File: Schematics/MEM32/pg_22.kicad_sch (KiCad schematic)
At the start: 6 parts, among them U1806 XLRULOGIC, U1901 F244, U1903 TSXXPAL, U1907 F258, U1908 F258, U2908 F64

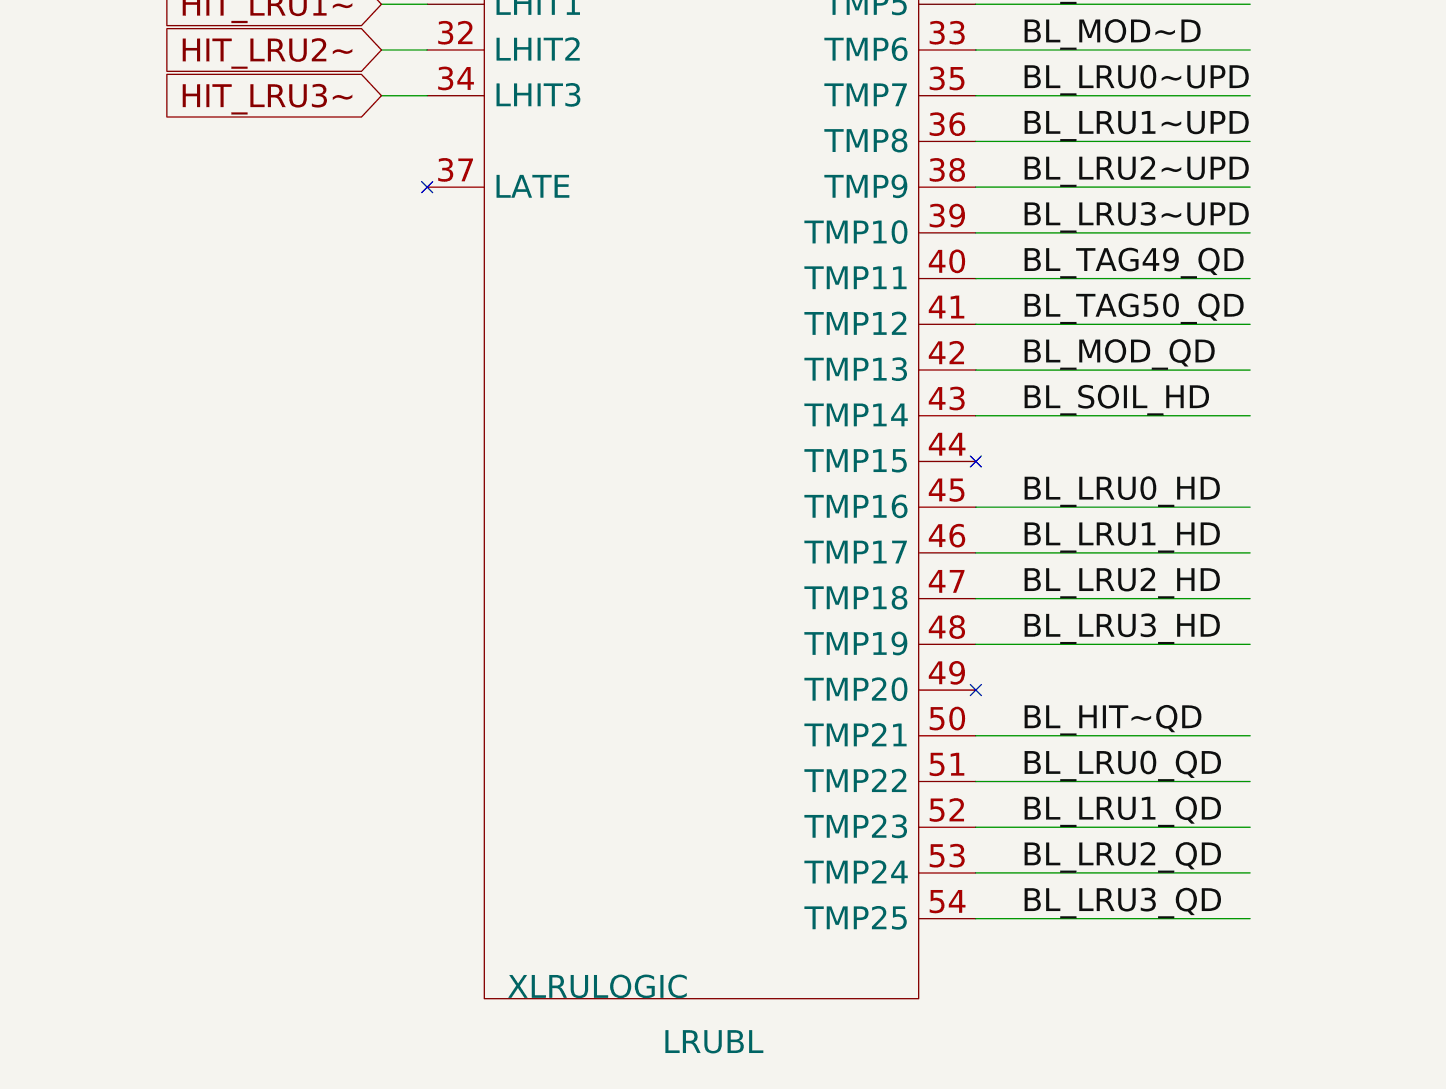
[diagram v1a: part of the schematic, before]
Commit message: MEM32: Eliminate MUXEPAL, tested to 16.8s (rm121)
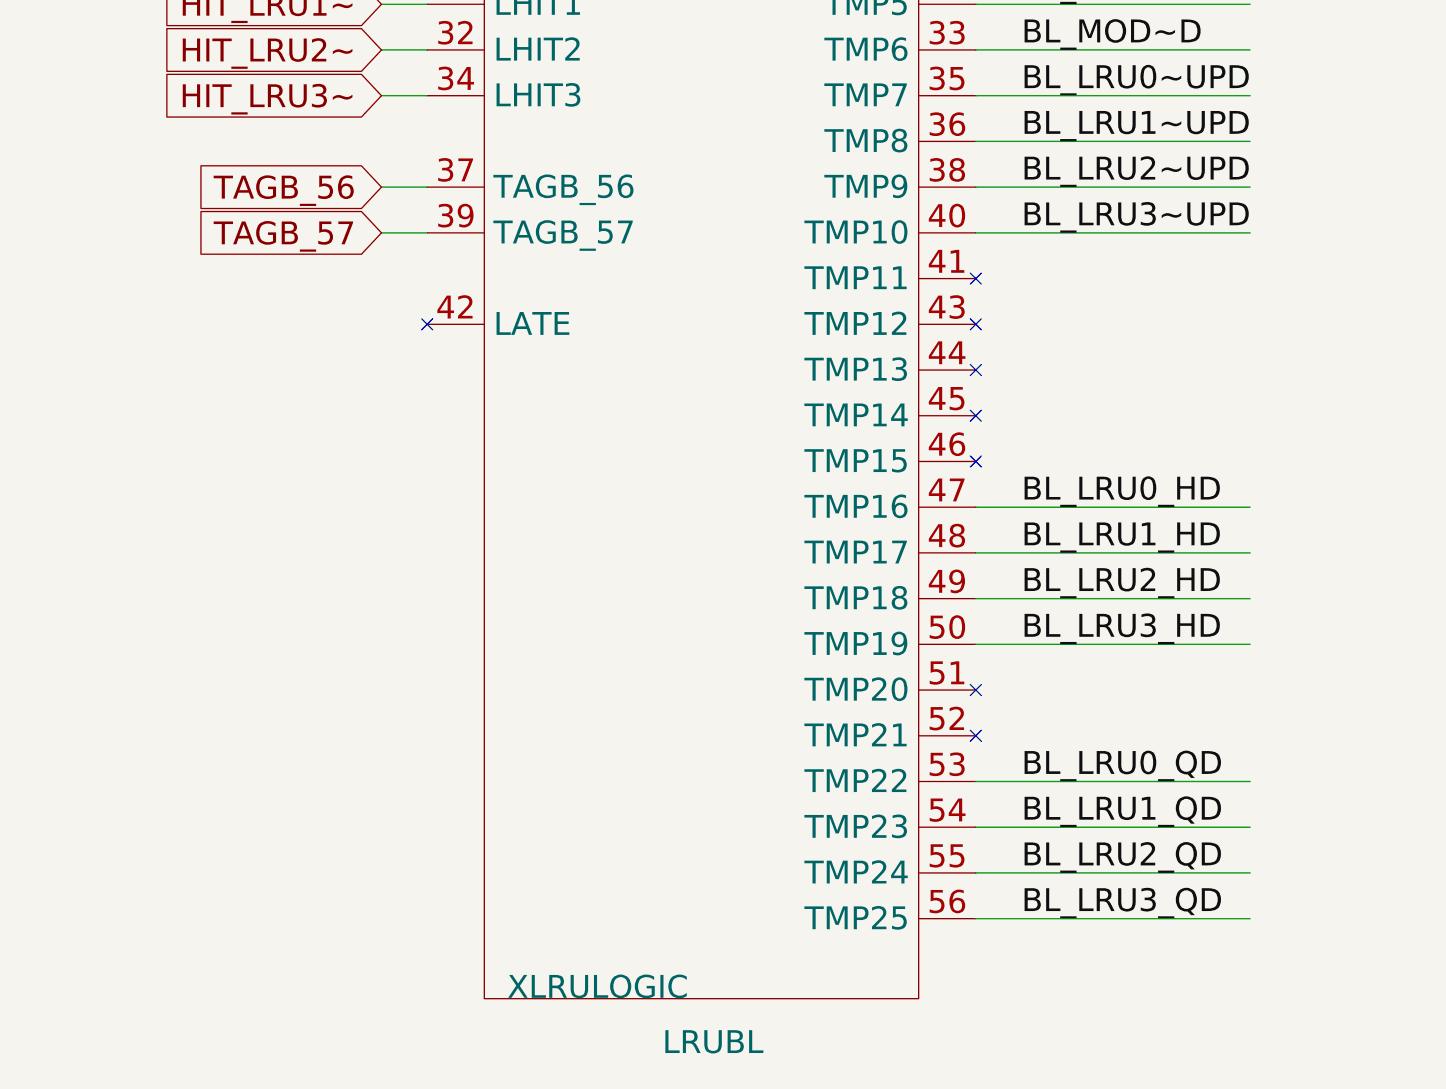
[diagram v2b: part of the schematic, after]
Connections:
- net BL_HIT~QD is gone; now on net BL_LRU3_HD: U1806.50 (TMP19)
- net BL_TAG49_QD is gone; now on net BL_LRU3~UPD: U1806.40 (TMP10)
- net BL_LRU0_HD: now also U1806.47 (TMP16); no longer U1806.45 (TMP16)
- net BL_LRU0_QD: now also U1806.53 (TMP22); no longer U1806.51 (TMP22)
- net BL_LRU1_HD: now also U1806.48 (TMP17); no longer U1806.46 (TMP17)
- net BL_LRU1_QD: now also U1806.54 (TMP23); no longer U1806.52 (TMP23)
- net BL_LRU2_HD: now also U1806.49 (TMP18); no longer U1806.47 (TMP18)
- net BL_LRU2_QD: now also U1806.55 (TMP24); no longer U1806.53 (TMP24)
- net BL_LRU3_HD: no longer U1806.48 (TMP19)
- net BL_LRU3_QD: now also U1806.56 (TMP25); no longer U1806.54 (TMP25)
- net BL_LRU3~UPD: no longer U1806.39 (TMP10)
- net TAGB_56: now also U1806.37 (TAGB_56)
- net TAGB_57: now also U1806.39 (TAGB_57)
- net BL_MOD_QD: no longer names the net of U1806.42 (LATE)
- net BL_SOIL_HD: no longer names the net of U1806.43 (TMP12)
- net BL_TAG50_QD: no longer names the net of U1806.41 (TMP11)
- no-connect marks 7 -> 12
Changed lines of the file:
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@@
   )
   (no_connect (at 152.4 71.12))
-  (no_connect (at 66.04 259.08))
+  (no_connect (at 66.04 274.32))
+  (no_connect (at 127 269.24))
   (no_connect (at 127 314.96))
   (no_connect (at 508 137.16))
+  (no_connect (at 127 274.32))
   (no_connect (at 508 43.18))
+  (no_connect (at 127 284.48))
   (no_connect (at 127 289.56))
   (no_connect (at 279.4 246.38))
+  (no_connect (at 127 320.04))
+  (no_connect (at 127 279.4))
   (bus_entry (at 68.58 63.5) (size 2.54 2.54)
     (stroke (width 0) (type default))
@@
     (stroke (width 0) (type default))
   )
+  (wire (pts (xy 60.96 264.16) (xy 66.04 264.16))
+    (stroke (width 0) (type default))
+  )
   (wire (pts (xy 472.44 93.98) (xy 495.3 93.98))
     (stroke (width 0) (type default))
@@
     (stroke (width 0) (type default))
   )
-  (wire (pts (xy 127 320.04) (xy 157.48 320.04))
-    (stroke (width 0) (type default))
-  )
   (wire (pts (xy 60.96 243.84) (xy 66.04 243.84))
     (stroke (width 0) (type default))
@@
     (stroke (width 0) (type default))
   )
-  (wire (pts (xy 127 284.48) (xy 157.48 284.48))
-    (stroke (width 0) (type default))
-  )
-  (wire (pts (xy 127 274.32) (xy 157.48 274.32))
-    (stroke (width 0) (type default))
-  )
   (wire (pts (xy 279.4 213.36) (xy 276.86 213.36))
     (stroke (width 0) (type default))
@@
     (stroke (width 0) (type default))
   )
+  (wire (pts (xy 60.96 259.08) (xy 66.04 259.08))
+    (stroke (width 0) (type default))
+  )
   (wire (pts (xy 71.12 71.12) (xy 114.3 71.12))
     (stroke (width 0) (type default))
@@
     (stroke (width 0) (type default))
   )
-  (wire (pts (xy 127 279.4) (xy 157.48 279.4))
-    (stroke (width 0) (type default))
-  )
   (bus (pts (xy 347.98 332.74) (xy 347.98 355.6))
     (stroke (width 0) (type default))
@@
     (stroke (width 0) (type default))
   )
-  (wire (pts (xy 127 269.24) (xy 157.48 269.24))
-    (stroke (width 0) (type default))
-  )
   (wire (pts (xy 233.68 355.6) (xy 264.16 355.6))
     (stroke (width 0) (type default))
@@
     (effects (font (size 2.54 2.54)) (justify left bottom))
   )
-  (label "BL_TAG50_QD" (at 132.08 274.32 0) (fields_autoplaced)
-    (effects (font (size 2.54 2.54)) (justify left bottom))
-  )
   (label "TAGBL_51" (at 132.08 147.32 0) (fields_autoplaced)
     (effects (font (size 2.54 2.54)) (justify left bottom))
@@
     (effects (font (size 2.54 2.54)) (justify left bottom))
   )
-  (label "BL_SOIL_HD" (at 132.08 284.48 0) (fields_autoplaced)
-    (effects (font (size 2.54 2.54)) (justify left bottom))
-  )
   (label "B_HTLRU3" (at 132.08 177.8 0) (fields_autoplaced)
     (effects (font (size 2.54 2.54)) (justify left bottom))
@@
     (effects (font (size 2.54 2.54)) (justify left bottom))
   )
-  (label "BL_HIT~QD" (at 132.08 320.04 0) (fields_autoplaced)
-    (effects (font (size 2.54 2.54)) (justify left bottom))
-  )
   (label "TAGBL_53" (at 543.56 165.1 0) (fields_autoplaced)
     (effects (font (size 2.54 2.54)) (justify left bottom))
   )
-  (label "BL_TAG49_QD" (at 132.08 269.24 0) (fields_autoplaced)
-    (effects (font (size 2.54 2.54)) (justify left bottom))
-  )
   (label "BL_LRU1_QD" (at 233.68 330.2 0) (fields_autoplaced)
     (effects (font (size 2.54 2.54)) (justify left bottom))
@@
   )
   (label "BL_LRU3_QD" (at 233.68 320.04 0) (fields_autoplaced)
-    (effects (font (size 2.54 2.54)) (justify left bottom))
-  )
-  (label "BL_MOD_QD" (at 132.08 279.4 0) (fields_autoplaced)
     (effects (font (size 2.54 2.54)) (justify left bottom))
   )
@@
     (property "Intersheetrefs" "${INTERSHEET_REFS}" (at 241.7337 261.62 0)
       (effects (font (size 1.27 1.27)) (justify right))
+    )
+  )
+  (global_label "TAGB_57" (shape input) (at 60.96 264.16 180) (fields_autoplaced)
+    (effects (font (size 2.54 2.54)) (justify right))
+    (property "Intersheet References" "${INTERSHEET_REFS}" (at 40.1683 264.0013 0)
+      (effects (font (size 1.905 1.905)) (justify right))
+    )
+  )
+  (global_label "TAGB_56" (shape input) (at 60.96 259.08 180) (fields_autoplaced)
+    (effects (font (size 2.54 2.54)) (justify right))
+    (property "Intersheet References" "${INTERSHEET_REFS}" (at 40.1683 258.9213 0)
+      (effects (font (size 1.905 1.905)) (justify right))
     )
   )
@@
     (pin "53")
     (pin "54")
+    (pin "55")
+    (pin "56")
     (pin "6")
     (pin "7")

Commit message: MEM32: Eliminate late B mux.  tested to 4.30 (rm124)
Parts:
- removed U1907, U1908: F258, symbol r1000:F258
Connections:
- net BL_LRU0~UPD: no longer names the net of U1806.35 (TMP7)
- net BL_LRU1~UPD: no longer names the net of U1806.36 (TMP8)
- net BL_LRU2~UPD: no longer names the net of U1806.38 (TMP9)
- net BL_LRU3~UPD: no longer names the net of U1806.40 (TMP10)
- net BL_MOD~D: no longer names the net of U1806.33 (TMP6)
- net BL_PAR~UPD: no longer names the net of U1806.27 (TMP3)
- net BL_TAG49~D: no longer names the net of U1806.29 (TMP4)
- net BL_TAG50~D: no longer names the net of U1806.31 (TMP5)
- net LRU_UPD_BOE~: no longer names the net of U1806.23 (TMP0)
- no-connect marks 12 -> 19
